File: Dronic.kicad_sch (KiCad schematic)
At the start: 56 parts, among them J1 SWDIO_PH_TERM, J2 Screw_Terminal_01x02, J3 JST_SH_6P_1.00mm, SW1 SW_Push, SW2 SW_Push, U1 RP2040, U2 2137160001, U3 W25Q128JVS, U4 LTC3521EFE-PBF, U5 AP62150WU, U6 ECH8690-TL-H, U8 NTJD5121NT1G, Y1 ABM3B-12.000MHZ-10-1-U-T

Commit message: Updates, intending on using the PCD8575 for I2C Motor Control
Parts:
- added U7, U9: PCF8575DBR, Package_SO:SSOP-24_5.3x8.2mm_P0.65mm, symbol Interface_Expansion:PCF8575DBR
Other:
- note added: "ADC | DAC"
- note added: "BLDC Motor Contoroller"
- note added: "Connector | Input"
- note added: "Memory | Oscillation"
- note added: "Power"
- note added: "The Goat - RP2040"

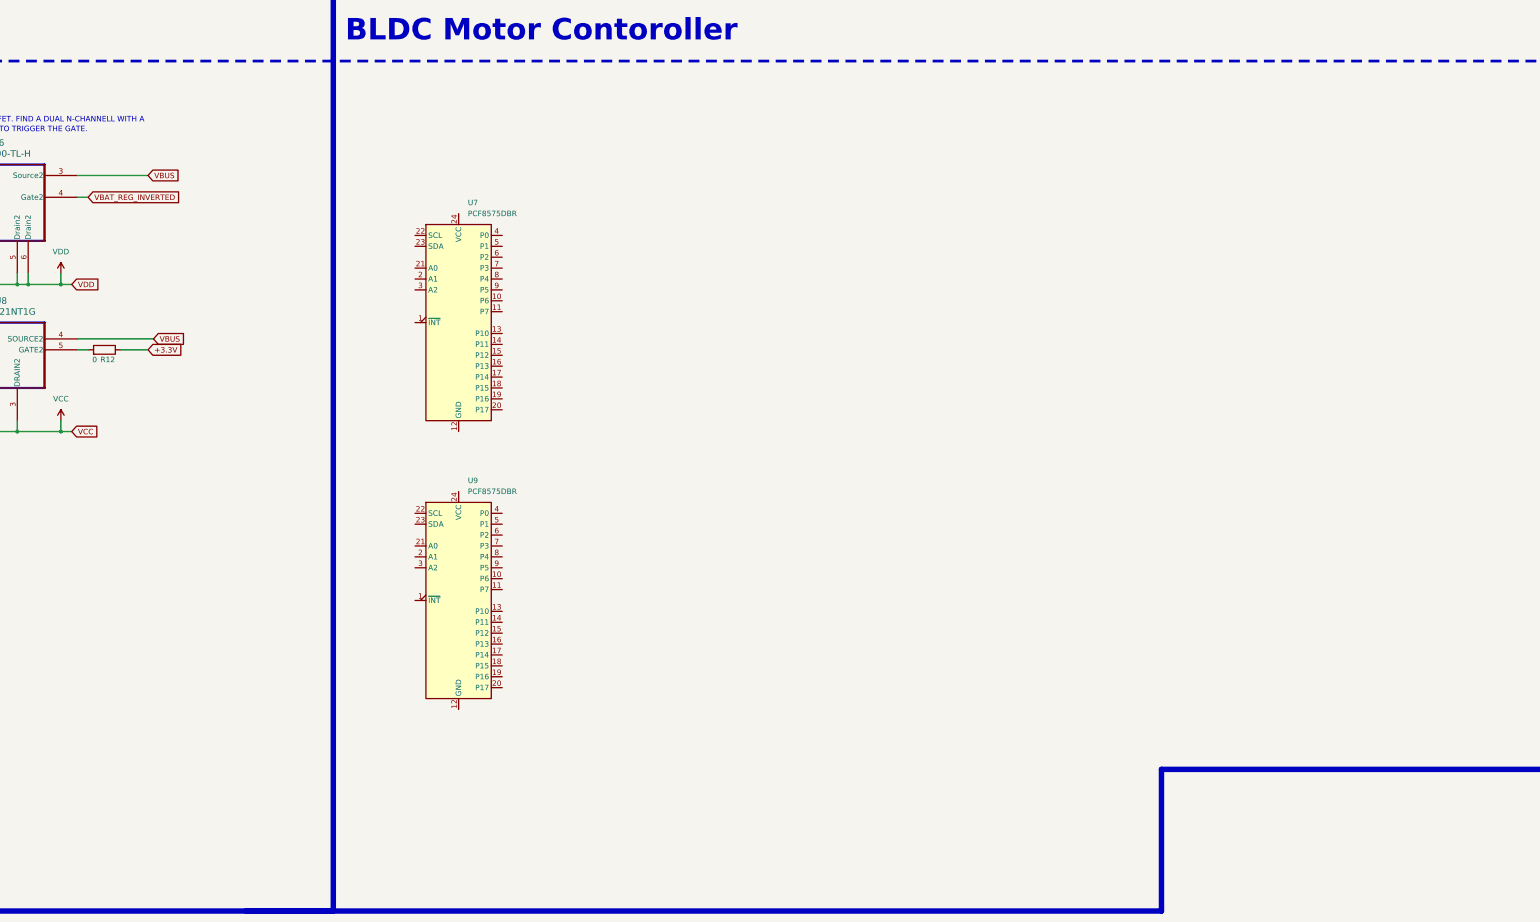
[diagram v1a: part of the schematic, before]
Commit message: Motor Controller Update
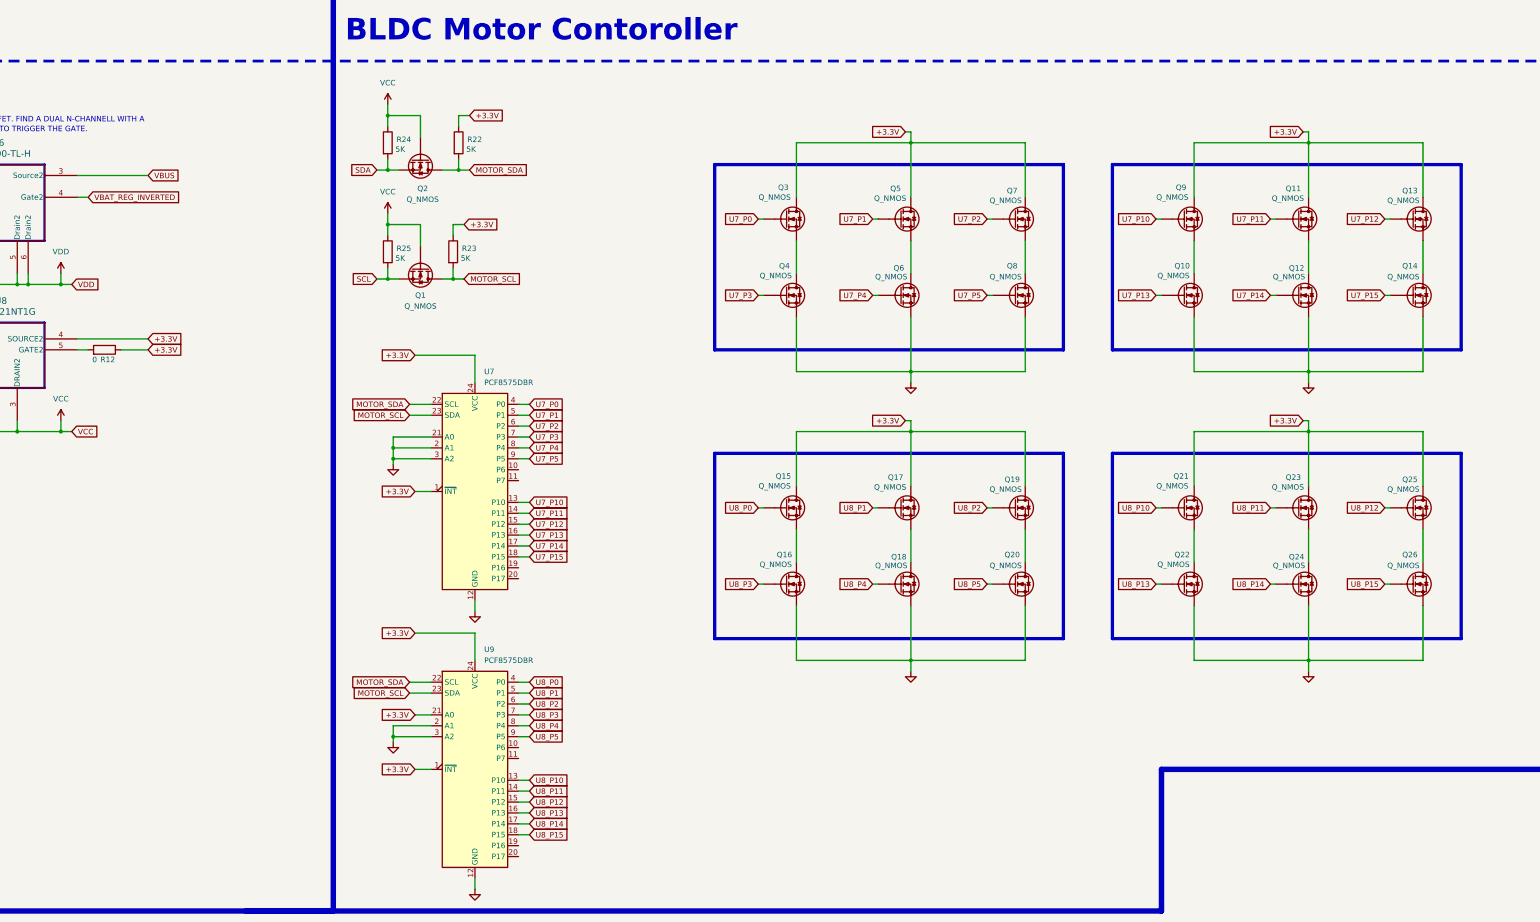
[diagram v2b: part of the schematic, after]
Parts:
- added Q1, Q10, Q11, Q12, Q13, Q14, Q15, Q16, Q17, Q18, Q19, Q2, Q20, Q21, Q22, Q23, Q24, Q25, Q26, Q3, Q4, Q5, Q6, Q7, Q8, Q9: Q_NMOS, symbol Device:Q_NMOS
- added R22, R23, R24, R25: 5K, Resistor_SMD:R_0402_1005Metric, symbol Device:R
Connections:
- net +3.3V: now also U7.1 (~{INT}), U7.24 (VCC), U8.4 (SOURCE2), U9.1 (~{INT}), U9.21 (A0), U9.24 (VCC), Q11.D, Q13.D, Q15.D, Q17.D, Q19.D, Q21.D, Q23.D, Q25.D, Q3.D, Q5.D, Q7.D, Q9.D, R22.1, R23.1
- net GND: now also U7.12 (GND), U7.2 (A1), U7.21 (A0), U7.3 (A2), U9.12 (GND), U9.2 (A1), U9.3 (A2), Q10.S, Q12.S, Q14.S, Q16.S, Q18.S, Q20.S, Q22.S, Q24.S, Q26.S, Q4.S, Q6.S, Q8.S
- net SCL: now also Q1.S, R25.2
- net SDA: now also Q2.S, R24.2
- net VBUS: no longer U8.4 (SOURCE2)
- net VCC: now also Q1.G, Q2.G, R24.1, R25.1
- net U8_P10: now reaches U9.13 (P10)
- net U8_P10: now also Q21.G
- net U8_P11: now reaches U9.14 (P11)
- net U8_P11: now also Q23.G
- net U8_P12: now reaches U9.15 (P12)
- net U8_P12: now also Q25.G
- net U8_P13: now reaches U9.16 (P13)
- net U8_P13: now also Q22.G
- net U8_P14: now reaches U9.17 (P14)
- net U8_P14: now also Q24.G
- net U8_P15: now reaches U9.18 (P15)
- net U8_P15: now also Q26.G
- net MOTOR_SDA: now reaches U9.22 (SCL)
- net MOTOR_SDA: now also U7.22 (SCL), Q2.D, R22.2
- net MOTOR_SCL: now reaches U9.23 (SDA)
- net MOTOR_SCL: now also U7.23 (SDA), Q1.D, R23.2
- net U8_P0: now reaches U9.4 (P0)
- net U8_P0: now also Q15.G
- net U8_P1: now reaches U9.5 (P1)
- net U8_P1: now also Q17.G
- net U8_P2: now reaches U9.6 (P2)
- net U8_P2: now also Q19.G
- net U8_P3: now reaches U9.7 (P3)
- net U8_P3: now also Q16.G
- net U8_P4: now reaches U9.8 (P4)
- net U8_P4: now also Q18.G
- net U8_P5: now reaches U9.9 (P5)
- net U8_P5: now also Q20.G
- net U7_P10: now reaches U7.13 (P10)
- net U7_P10: now also Q9.G
- net U7_P11: now reaches U7.14 (P11)
- net U7_P11: now also Q11.G
- net U7_P12: now reaches U7.15 (P12)
- net U7_P12: now also Q13.G
- net U7_P13: now reaches U7.16 (P13)
- net U7_P13: now also Q10.G
- net U7_P14: now reaches U7.17 (P14)
- net U7_P14: now also Q12.G
- net U7_P15: now reaches U7.18 (P15)
- net U7_P15: now also Q14.G
- net U7_P0: now reaches U7.4 (P0)
- net U7_P0: now also Q3.G
- net U7_P1: now reaches U7.5 (P1)
- net U7_P1: now also Q5.G
- net U7_P2: now reaches U7.6 (P2)
- net U7_P2: now also Q7.G
- net U7_P3: now reaches U7.7 (P3)
- net U7_P3: now also Q4.G
- net U7_P4: now reaches U7.8 (P4)
- net U7_P4: now also Q6.G
- net U7_P5: now reaches U7.9 (P5)
- net U7_P5: now also Q8.G
- new net: Q21.S, Q22.D
- new net: Q5.S, Q6.D
- new net: Q15.S, Q16.D
- new net: Q7.S, Q8.D
- new net: Q19.S, Q20.D
- new net: Q11.S, Q12.D
- new net: Q13.S, Q14.D
- new net: Q10.D, Q9.S
- new net: Q17.S, Q18.D
- new net: Q23.S, Q24.D
- new net: Q25.S, Q26.D
- new net: Q3.S, Q4.D
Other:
- moved on the sheet: U7, U9

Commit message: Title and Clean Up
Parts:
- added J4, J5, J6, J7: Screw_Terminal_01x03, symbol Connector:Screw_Terminal_01x03
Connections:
- net +11.1V: now also Q11.D, Q13.D, Q15.D, Q17.D, Q19.D, Q21.D, Q23.D, Q25.D, Q3.D, Q5.D, Q7.D, Q9.D
- net +3.3V: no longer Q11.D, Q13.D, Q15.D, Q17.D, Q19.D, Q21.D, Q23.D, Q25.D, Q3.D, Q5.D, Q7.D, Q9.D
- net at Q21.S, Q22.D: now also J5.3 (Pin_3)
- net at Q5.S, Q6.D: now also J6.2 (Pin_2)
- net at Q15.S, Q16.D: now also J7.3 (Pin_3)
- net at Q7.S, Q8.D: now also J6.1 (Pin_1)
- net at Q19.S, Q20.D: now also J7.1 (Pin_1)
- net at Q11.S, Q12.D: now also J4.2 (Pin_2)
- net at Q13.S, Q14.D: now also J4.1 (Pin_1)
- net at Q10.D, Q9.S: now also J4.3 (Pin_3)
- net at Q17.S, Q18.D: now also J7.2 (Pin_2)
- net at Q23.S, Q24.D: now also J5.2 (Pin_2)
- net at Q25.S, Q26.D: now also J5.1 (Pin_1)
- net at Q3.S, Q4.D: now also J6.3 (Pin_3)
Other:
- note added: "DRONIC"
- note added: "NickyWicky EE"
- note added: "github.com/NickyWicky34/Dronic/"
- moved on the sheet: Q15, Q16, Q17, Q18, Q19, Q20, Q3, Q4, Q5, Q6, Q7, Q8

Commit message: Added new parts, Edited Schematic
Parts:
- added IC1, IC10, IC11, IC12, IC2, IC3, IC4, IC5, IC6, IC7, IC8, IC9: ACS71240LLCBTR-050U5, SOIC127P600X175-8N, symbol ACS71240LLCBTR-050U5:ACS71240LLCBTR-050U5
- added Q27, Q28: Q_NMOS, symbol Device:Q_NMOS
- added R26, R27, R28, R29: 5K, Resistor_SMD:R_0402_1005Metric, symbol Device:R
- added U10: MAX11616, Package_SO:QSOP-16_3.9x4.9mm_P0.635mm, symbol Analog_ADC:MAX11616
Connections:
- net GND: now also IC1.5 (GND), IC10.5 (GND), IC11.5 (GND), IC12.5 (GND), IC2.5 (GND), IC3.5 (GND), IC4.5 (GND), IC5.5 (GND), IC6.5 (GND), IC7.5 (GND), IC8.5 (GND), IC9.5 (GND), U10.15 (GND)
- net SCL: now also Q28.S, R27.2
- net SDA: now also Q27.S, R26.2
- net VBAT_REG: now also IC1.8 (VCC), IC10.8 (VCC), IC11.8 (VCC), IC12.8 (VCC), IC2.8 (VCC), IC3.8 (VCC), IC4.8 (VCC), IC5.8 (VCC), IC6.8 (VCC), IC7.8 (VCC), IC8.8 (VCC), IC9.8 (VCC), R28.1, R29.1, U10.16 (Vdd)
- net VCC: now also Q27.G, Q28.G, R26.1, R27.1
- net -M4_W: now reaches Q21.S, Q22.D
- net -M4_W: now also IC12.3 (IP-_1), IC12.4 (IP-_2); no longer J5.3 (Pin_3)
- net -M1_U: now reaches Q7.S, Q8.D
- net -M1_U: now also IC1.3 (IP-_1), IC1.4 (IP-_2); no longer J6.1 (Pin_1)
- net -M1_V: now reaches Q5.S, Q6.D
- net -M1_V: now also IC2.3 (IP-_1), IC2.4 (IP-_2); no longer J6.2 (Pin_2)
- net -M1_W: now reaches Q3.S, Q4.D
- net -M1_W: now also IC3.3 (IP-_1), IC3.4 (IP-_2); no longer J6.3 (Pin_3)
- net -M4_U: now reaches Q25.S, Q26.D
- net -M4_U: now also IC10.3 (IP-_1), IC10.4 (IP-_2); no longer J5.1 (Pin_1)
- net -M4_V: now reaches Q23.S, Q24.D
- net -M4_V: now also IC11.3 (IP-_1), IC11.4 (IP-_2); no longer J5.2 (Pin_2)
- net -M2_W: now reaches Q15.S, Q16.D
- net -M2_W: now also IC9.3 (IP-_1), IC9.4 (IP-_2); no longer J7.3 (Pin_3)
- net -M2_U: now reaches Q19.S, Q20.D
- net -M2_U: now also IC7.3 (IP-_1), IC7.4 (IP-_2); no longer J7.1 (Pin_1)
- net -M3_V: now reaches Q11.S, Q12.D
- net -M3_V: now also IC5.3 (IP-_1), IC5.4 (IP-_2); no longer J4.2 (Pin_2)
- net -M2_V: now reaches Q17.S, Q18.D
- net -M2_V: now also IC8.3 (IP-_1), IC8.4 (IP-_2); no longer J7.2 (Pin_2)
- net -M3_U: now reaches Q13.S, Q14.D
- net -M3_U: now also IC4.3 (IP-_1), IC4.4 (IP-_2); no longer J4.1 (Pin_1)
- net -M3_W: now reaches Q10.D, Q9.S
- net -M3_W: now also IC6.3 (IP-_1), IC6.4 (IP-_2); no longer J4.3 (Pin_3)
- net U8_P6: now reaches U9.10 (P6)
- net U8_P6: now also IC4.6 (~{FAULT}), IC5.6 (~{FAULT}), IC6.6 (~{FAULT})
- net U8_P7: now reaches U9.11 (P7)
- net U8_P7: now also IC10.6 (~{FAULT}), IC11.6 (~{FAULT}), IC12.6 (~{FAULT})
- net U7_P6: now reaches U7.10 (P6)
- net U7_P6: now also IC1.6 (~{FAULT}), IC2.6 (~{FAULT}), IC3.6 (~{FAULT})
- net U7_P7: now reaches U7.11 (P7)
- net U7_P7: now also IC7.6 (~{FAULT}), IC8.6 (~{FAULT}), IC9.6 (~{FAULT})
- new net +M1_U: IC1.1 (IP+_1), IC1.2 (IP+_2)
- new net +M1_V: IC2.1 (IP+_1), IC2.2 (IP+_2)
- new net +M1_W: IC3.1 (IP+_1), IC3.2 (IP+_2)
- new net +M2_U: IC7.1 (IP+_1), IC7.2 (IP+_2)
- new net +M2_V: IC8.1 (IP+_1), IC8.2 (IP+_2)
- new net +M2_W: IC9.1 (IP+_1), IC9.2 (IP+_2)
- new net +M3_U: IC4.1 (IP+_1), IC4.2 (IP+_2)
- new net +M3_V: IC5.1 (IP+_1), IC5.2 (IP+_2)
- new net +M3_W: IC6.1 (IP+_1), IC6.2 (IP+_2)
- new net +M4_U: IC10.1 (IP+_1), IC10.2 (IP+_2)
- new net +M4_V: IC11.1 (IP+_1), IC11.2 (IP+_2)
- new net +M4_W: IC12.1 (IP+_1), IC12.2 (IP+_2)
- new net ADC_SCL: Q28.D, R28.2, U10.13 (SCL)
- new net ADC_SDA: Q27.D, R29.2, U10.14 (SDA)
- new net AIN0: IC1.7 (VIOUT), U10.5 (AIN0)
- new net AIN1: IC2.7 (VIOUT), U10.6 (AIN1)
- new net AIN10: IC11.7 (VIOUT), U10.2 (AIN10)
- new net AIN11: IC12.7 (VIOUT), U10.1 (AIN11)
- new net AIN2: IC3.7 (VIOUT), U10.7 (AIN2)
- new net AIN3: IC7.7 (VIOUT), U10.8 (AIN3)
- new net AIN4: IC8.7 (VIOUT), U10.9 (AIN4)
- new net AIN5: IC9.7 (VIOUT), U10.10 (AIN5)
- new net AIN6: IC4.7 (VIOUT), U10.11 (AIN6)
- new net AIN7: IC5.7 (VIOUT), U10.12 (AIN7)
- new net AIN8: IC6.7 (VIOUT), U10.4 (AIN8)
- new net AIN9: IC10.7 (VIOUT), U10.3 (AIN9)
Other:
- note added: "ADC"
- note added: "C_SENSE-1"
- note added: "C_SENSE-2"
- note added: "C_SENSE-3"
- note added: "C_SENSE-4"
- note added: "LEVEL SHIFT"
- note added: "MOTOR-1"
- note added: "MOTOR-2"
- note added: "MOTOR-3"
- note added: "MOTOR-4"
- note added: "Memory | Oscillator"
- note removed: "ADC | DAC"
- note removed: "Memory | Oscillation"
- moved on the sheet: C13, C14, D2, D3, D4, J2, J3, J4, L4, Q1, Q10, Q11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

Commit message: Schematic Clean-Up and added XBEE Module
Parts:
- added IC13: XBP9B-XCWT-001, XBP9BXCWT001, symbol XBP9B-XCWT-001:XBP9B-XCWT-001
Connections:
- net +M1_U: now also J4.1 (Pin_1)
- net +M1_V: now also J4.2 (Pin_2)
- net +M1_W: now also J4.3 (Pin_3)
- net +M2_U: now also J5.1 (Pin_1)
- net +M2_V: now also J5.2 (Pin_2)
- net +M2_W: now also J5.3 (Pin_3)
- net +M3_U: now also J6.1 (Pin_1)
- net +M3_V: now also J6.2 (Pin_2)
- net +M3_W: now also J6.3 (Pin_3)
- net +M4_U: now also J7.1 (Pin_1)
- net +M4_V: now also J7.2 (Pin_2)
- net +M4_W: now also J7.3 (Pin_3)
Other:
- note added: "XBEE"
- moved on the sheet: C10, C11, C12, C4, C5, C6, C7, C8, C9, J1, J4, Q27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
